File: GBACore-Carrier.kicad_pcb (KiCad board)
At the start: 2 copper layers, 2 parts, among them J1 BM24-40DS_2-0.35V_53_, J2 BM24-40DS_2-0.35V_53_

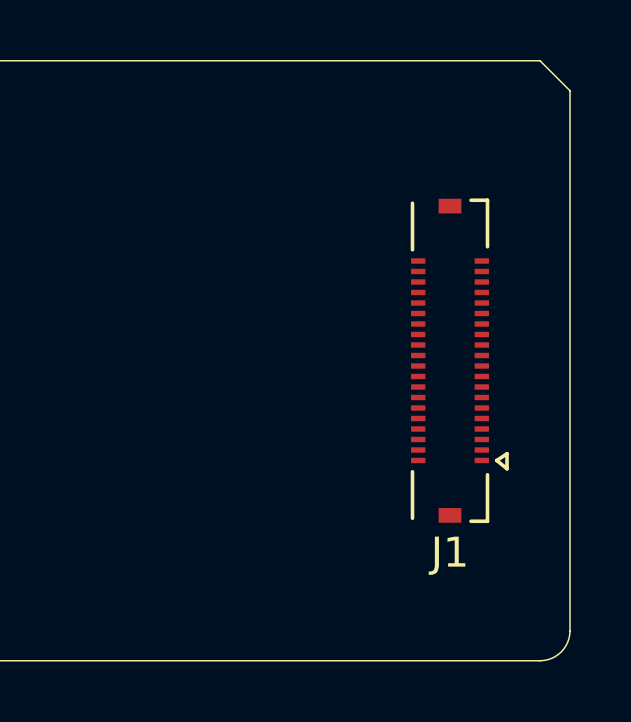
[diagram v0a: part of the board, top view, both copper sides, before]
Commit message: Update pinout
V0.99 Pinout (Final?)
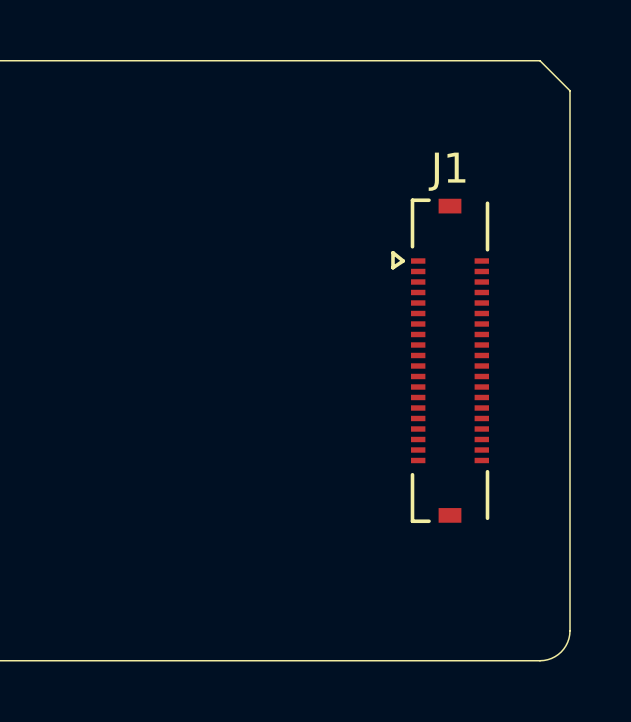
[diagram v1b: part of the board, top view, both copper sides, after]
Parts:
- turned J1 to 0 degrees
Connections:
- J1 pad 1: RESET -> AD10
- J1 pad 10: IN35 -> AD15
- J1 pad 11: IRQ/DREQ -> AD5
- J1 pad 12: PHI -> A16
- J1 pad 13: ~{CS2} -> AD4
- J1 pad 14: ~{WR} -> A17
- J1 pad 15: A23 -> AD3
- J1 pad 16: ~{RD} -> A18
- J1 pad 17: A22 -> AD2
- J1 pad 18: ~{CS1} -> A19
- J1 pad 19: A21 -> AD1
- J1 pad 2: SO -> AD11
- J1 pad 20: AD0 -> A20
- J1 pad 21: A20 -> AD0
- J1 pad 22: AD1 -> A21
- J1 pad 23: A19 -> ~{CS1}
- J1 pad 24: AD2 -> A22
- J1 pad 25: A18 -> ~{RD}
- J1 pad 26: AD3 -> A23
- J1 pad 27: A17 -> ~{WR}
- J1 pad 28: AD4 -> ~{CS2}
- J1 pad 29: A16 -> PHI
- J1 pad 3: GND -> AD9
- J1 pad 30: AD5 -> IRQ/DREQ
- J1 pad 31: AD15 -> GND
- J1 pad 32: AD6 -> GND
- J1 pad 33: AD14 -> SC
- J1 pad 34: AD7 -> GND
- J1 pad 35: AD13 -> SD
- J1 pad 36: AD8 -> GND
- J1 pad 37: AD12 -> SI
- J1 pad 38: AD9 -> GND
- J1 pad 39: AD11 -> SO
- J1 pad 4: SI -> AD12
- J1 pad 40: AD10 -> RESET
- J1 pad 41: IN35 -> +3V3
- J1 pad 42: +3V3 -> IN35
- J1 pad 5: GND -> AD8
- J1 pad 6: SD -> AD13
- J1 pad 7: GND -> AD7
- J1 pad 8: SC -> AD14
- J1 pad 9: GND -> AD6
- J2 pad 34: GND -> unconnected-(J2-Pad34)
- J2 pad 36: GND -> CK2
- J2 pad 38: GND -> CK1
- J2 pad 40: GND -> unconnected-(J2-Pad40)

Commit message: Fix orientation of J1
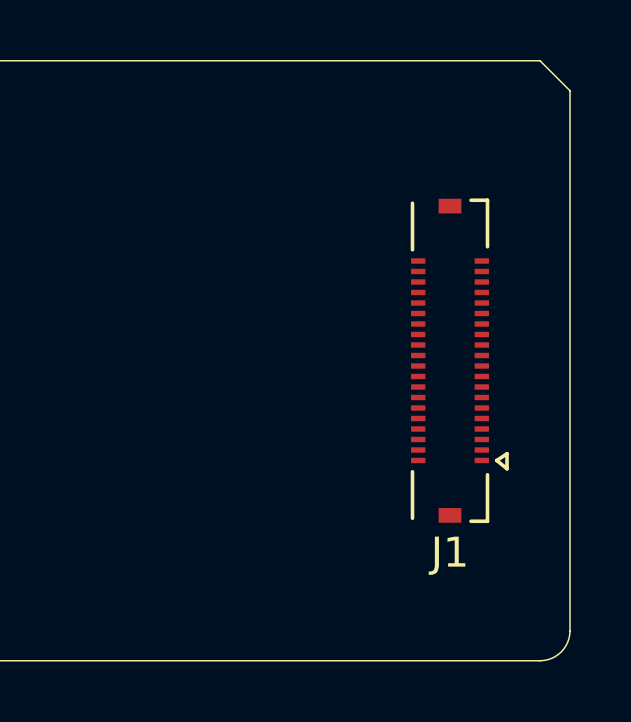
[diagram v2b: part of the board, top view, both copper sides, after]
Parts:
- turned J1 to 180 degrees
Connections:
- J1 pad 1: AD10 -> RESET
- J1 pad 10: AD15 -> GND
- J1 pad 11: AD5 -> IRQ/DREQ
- J1 pad 12: A16 -> PHI
- J1 pad 13: AD4 -> ~{CS2}
- J1 pad 14: A17 -> ~{WR}
- J1 pad 15: AD3 -> A23
- J1 pad 16: A18 -> ~{RD}
- J1 pad 17: AD2 -> A22
- J1 pad 18: A19 -> ~{CS1}
- J1 pad 19: AD1 -> A21
- J1 pad 2: AD11 -> SO
- J1 pad 20: A20 -> AD0
- J1 pad 21: AD0 -> A20
- J1 pad 22: A21 -> AD1
- J1 pad 23: ~{CS1} -> A19
- J1 pad 24: A22 -> AD2
- J1 pad 25: ~{RD} -> A18
- J1 pad 26: A23 -> AD3
- J1 pad 27: ~{WR} -> A17
- J1 pad 28: ~{CS2} -> AD4
- J1 pad 29: PHI -> A16
- J1 pad 3: AD9 -> GND
- J1 pad 30: IRQ/DREQ -> AD5
- J1 pad 31: GND -> AD15
- J1 pad 32: GND -> AD6
- J1 pad 33: SC -> AD14
- J1 pad 34: GND -> AD7
- J1 pad 35: SD -> AD13
- J1 pad 36: GND -> AD8
- J1 pad 37: SI -> AD12
- J1 pad 38: GND -> AD9
- J1 pad 39: SO -> AD11
- J1 pad 4: AD12 -> SI
- J1 pad 40: RESET -> AD10
- J1 pad 41: +3V3 -> IN35
- J1 pad 42: IN35 -> +3V3
- J1 pad 5: AD8 -> GND
- J1 pad 6: AD13 -> SD
- J1 pad 7: AD7 -> GND
- J1 pad 8: AD14 -> SC
- J1 pad 9: AD6 -> GND
